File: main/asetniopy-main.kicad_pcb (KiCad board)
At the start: 2 copper layers, 32 x 33 mm, 19 parts, among them J1 Conn_01x02, J2 Conn_01x02, J3 Conn_01x02, J4 Conn_01x02, J5 Conn_01x02, J6 Power/Reset, J7 BAT+, J8 BAT-, U1 ProMicro, U2 LIS2DW12

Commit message: More parts, rotation/placement fixes.
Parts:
- turned C2 to -90 degrees
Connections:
- C2 pad 1: VCC -> GND
- C2 pad 2: GND -> VCC
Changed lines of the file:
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@@
   (net 12 "unconnected-(U1-Pad10)")
   (net 13 "unconnected-(U2-Pad5)")
-  (net 14 "Net-(U1-Pad24)")
+  (net 14 "Net-(J7-Pad1)")
   (net 15 "BAT-")
   (net 16 "RESET")
@@
       (net 1 "GND") (pinfunction "GND") (pintype "input"))
     (pad "24" thru_hole circle (at -13.97 -7.62 270) (size 1.7526 1.7526) (drill 1.0922) (layers *.Cu *.SilkS *.Mask)
-      (net 14 "Net-(U1-Pad24)") (pinfunction "RAW") (pintype "input"))
+      (net 14 "Net-(J7-Pad1)") (pinfunction "RAW") (pintype "input"))
     (model "/Users/danny/Documents/proj/custom-keyboard/kicad-libs/3d_models/ArduinoProMicro.wrl"
       (offset (xyz -13.96999979 -7.619999886 -5.841999912))
@@
     (fp_line (start -1.27 1.27) (end -1.27 -1.27) (layer "F.Fab") (width 0.1))
     (pad "1" thru_hole circle (at 0.0345 0) (size 1.7 1.7) (drill 1) (layers *.Cu *.Mask)
-      (net 14 "Net-(U1-Pad24)") (pinfunction "Pin_1") (pintype "passive"))
+      (net 14 "Net-(J7-Pad1)") (pinfunction "Pin_1") (pintype "passive"))
   )
   (footprint "MountingHole:MountingHole_2.2mm_M2_Pad" (layer "F.Cu")
@@
   )
   (footprint "Capacitor_Tantalum_SMD:CP_EIA-3216-18_Kemet-A" (layer "B.Cu")
-    (at 99.625 113.15 90)
+    (at 99.625 113.15 -90)
     (descr "Tantalum Capacitor SMD Kemet-A (3216-18 Metric), IPC_7351 nominal, (Body size from: http://www.kemet.com/Lists/ProductCatalog/Attachments/253/KEM_TC101_STD.pdf), generated with kicad-footprint-generator")
     (tags "capacitor tantalum")
+    (property "LCSC Part Number" "C7171")
     (property "Sheetfile" "asetniopy-main.kicad_sch")
     (property "Sheetname" "")
     (attr smd)
-    (fp_text reference "C2" (at -2.15 -2.075 180) (layer "B.SilkS")
+    (fp_text reference "C2" (at -2.15 -2.075) (layer "B.SilkS")
       (effects (font (size 1 1) (thickness 0.15)) (justify mirror))
     )
@@
     (fp_line (start -1.6 -0.8) (end 1.6 -0.8) (layer "B.Fab") (width 0.1))
     (fp_line (start 1.6 0.8) (end -1.2 0.8) (layer "B.Fab") (width 0.1))
-    (pad "1" smd roundrect (at -1.35 0 90) (size 1.4 1.35) (layers "B.Cu" "B.Paste" "B.Mask") (roundrect_rratio 0.185185)
+    (pad "1" smd roundrect (at -1.35 0 270) (size 1.4 1.35) (layers "B.Cu" "B.Paste" "B.Mask") (roundrect_rratio 0.185185)
+      (net 1 "GND") (pintype "passive"))
+    (pad "2" smd roundrect (at 1.35 0 270) (size 1.4 1.35) (layers "B.Cu" "B.Paste" "B.Mask") (roundrect_rratio 0.185185)
       (net 2 "VCC") (pintype "passive"))
-    (pad "2" smd roundrect (at 1.35 0 90) (size 1.4 1.35) (layers "B.Cu" "B.Paste" "B.Mask") (roundrect_rratio 0.185185)
-      (net 1 "GND") (pintype "passive"))
     (model "${KICAD6_3DMODEL_DIR}/Capacitor_Tantalum_SMD.3dshapes/CP_EIA-3216-18_Kemet-A.wrl"
       (offset (xyz 0 0 0))
@@
     (descr "LGA12")
     (tags "lga land grid array")
+    (property "LCSC Part Number" "C189624")
     (property "Sheetfile" "asetniopy-main.kicad_sch")
     (property "Sheetname" "")
@@
     (descr "Capacitor SMD 0603 (1608 Metric), square (rectangular) end terminal, IPC_7351 nominal, (Body size source: IPC-SM-782 page 76, https://www.pcb-3d.com/wordpress/wp-content/uploads/ipc-sm-782a_amendment_1_and_2.pdf), generated with kicad-footprint-generator")
     (tags "capacitor")
+    (property "LCSC Part Number" "C14663")
     (property "Sheetfile" "asetniopy-main.kicad_sch")
     (property "Sheetname" "")
@@
     (descr "Capacitor SMD 0603 (1608 Metric), square (rectangular) end terminal, IPC_7351 nominal, (Body size source: IPC-SM-782 page 76, https://www.pcb-3d.com/wordpress/wp-content/uploads/ipc-sm-782a_amendment_1_and_2.pdf), generated with kicad-footprint-generator")
     (tags "capacitor")
-    (property "Sheetfile" "asetniopy-main.kicad_sch")
-    (property "Sheetname" "")
+    (property "LCSC Part Number" "C14663")
+    (property "Sheetfile" "asetniopy-main.kicad_sch")
+    (property "Sheetname" "")

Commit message: Timestamps
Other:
- board text added: "By: @petejohanson Commit: ${COMMIT}"
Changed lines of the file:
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@@
     )
   )
+  (property "COMMIT" "deadbeef")
   (net 0 "")
   (net 1 "GND")
@@
   (gr_line (start 89 89.5) (end 87 89.5) (layer "Edge.Cuts") (width 0.1))
   (gr_arc (start 113 83.5) (mid 116 86.5) (end 113 89.5) (layer "Edge.Cuts") (width 0.1))
+  (gr_text "By:\n@petejohanson\nCommit:\n${COMMIT}" (at 98.975 104.625 90) (layer "F.SilkS")
+    (effects (font (size 1 1) (thickness 0.15)) (justify left))
+  )
   (via (at 110.225 115.475) (size 0.8) (drill 0.4) (layers "F.Cu" "B.Cu") (free) (net 1))
   (via (at 96.125 114.95) (size 0.8) (drill 0.4) (layers "F.Cu" "B.Cu") (free) (net 1))

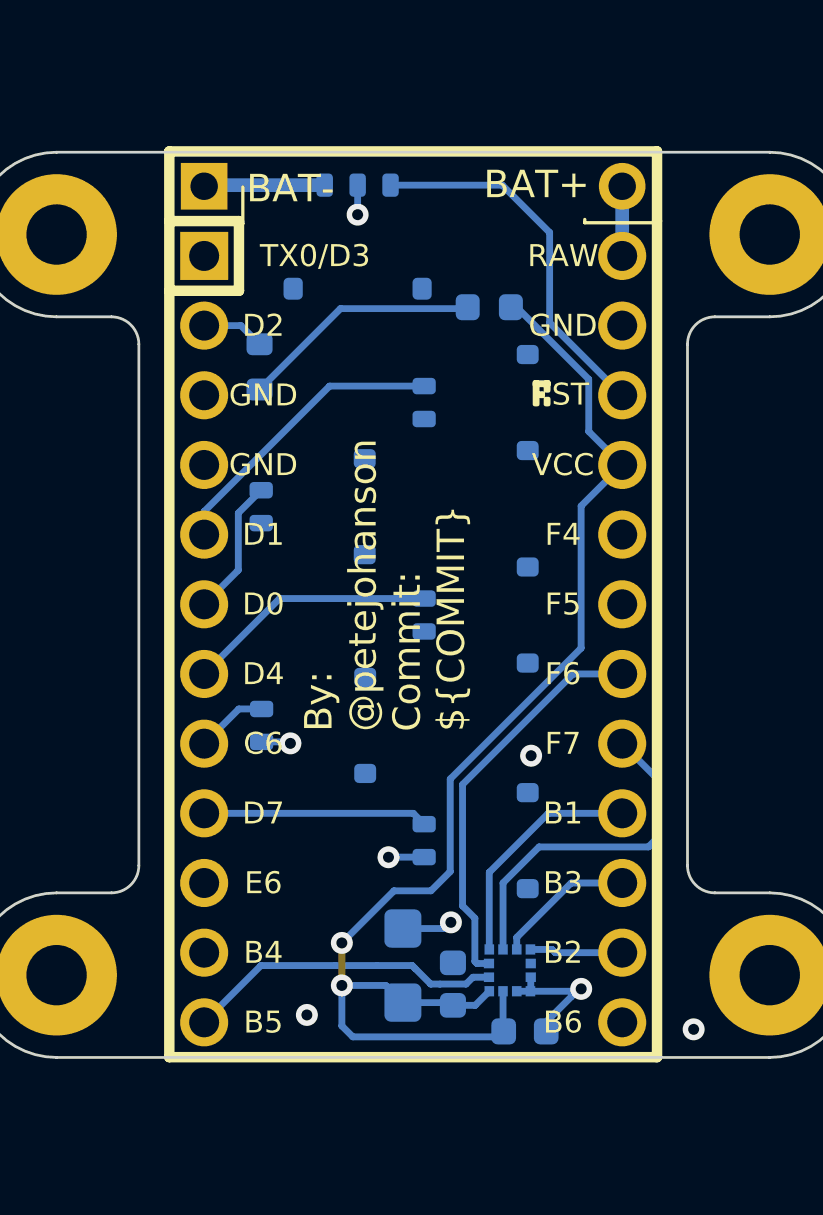
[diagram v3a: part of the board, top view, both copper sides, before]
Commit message: Minor placement/silk tweaks.
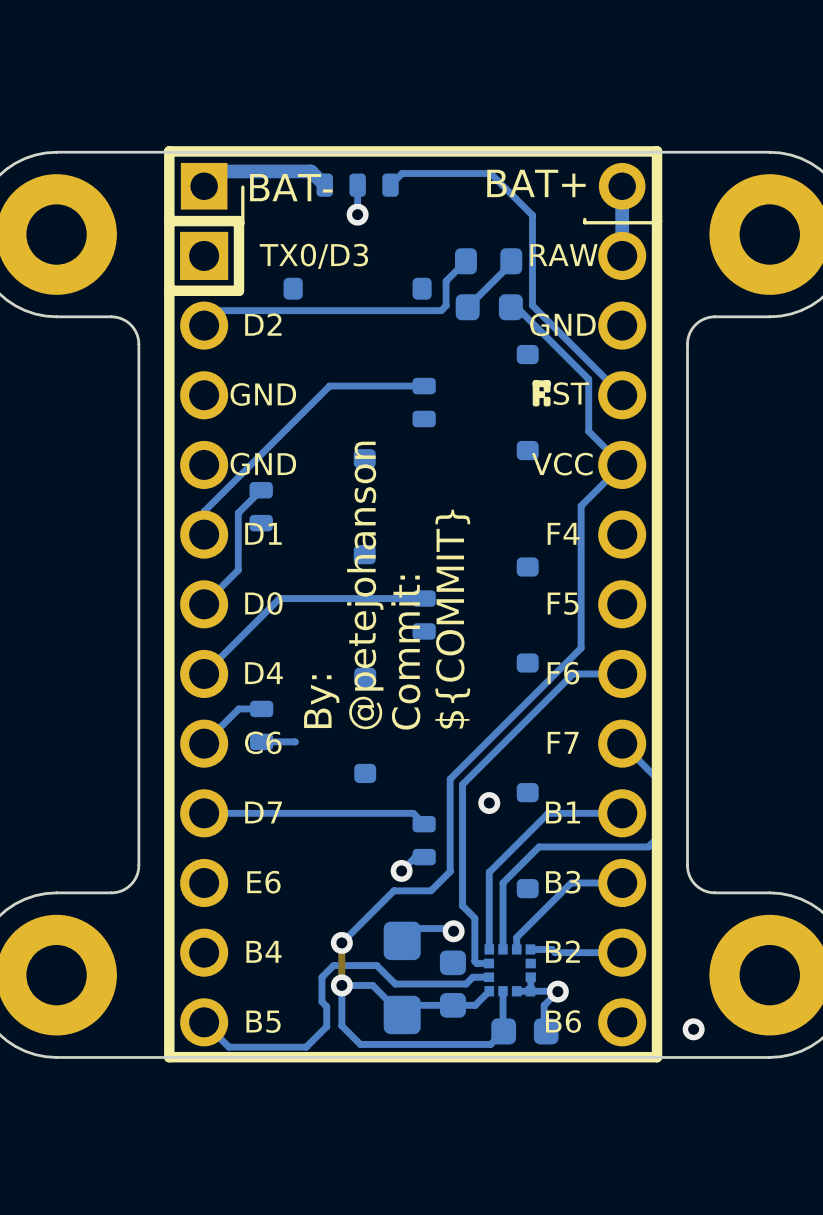
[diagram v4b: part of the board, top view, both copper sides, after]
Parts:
- D1: value User -> Blue
- R1: value 120 -> 68
- moved R1 9.19 mm to (102.8, 87.5), turned to 0 degrees
- moved C2 0.45 mm to (99.6, 113.6)
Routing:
- net LED: track 2.30 -> 11.0 mm
- net Net-(D1-Pad1): track 8.83 -> 2.33 mm
- net ACC_INT2: track 11.6 -> 13.7 mm
- net GND: track 10.6 -> 8.93 mm, vias 8 -> 6
- net VCC: track 46.3 -> 47.0 mm

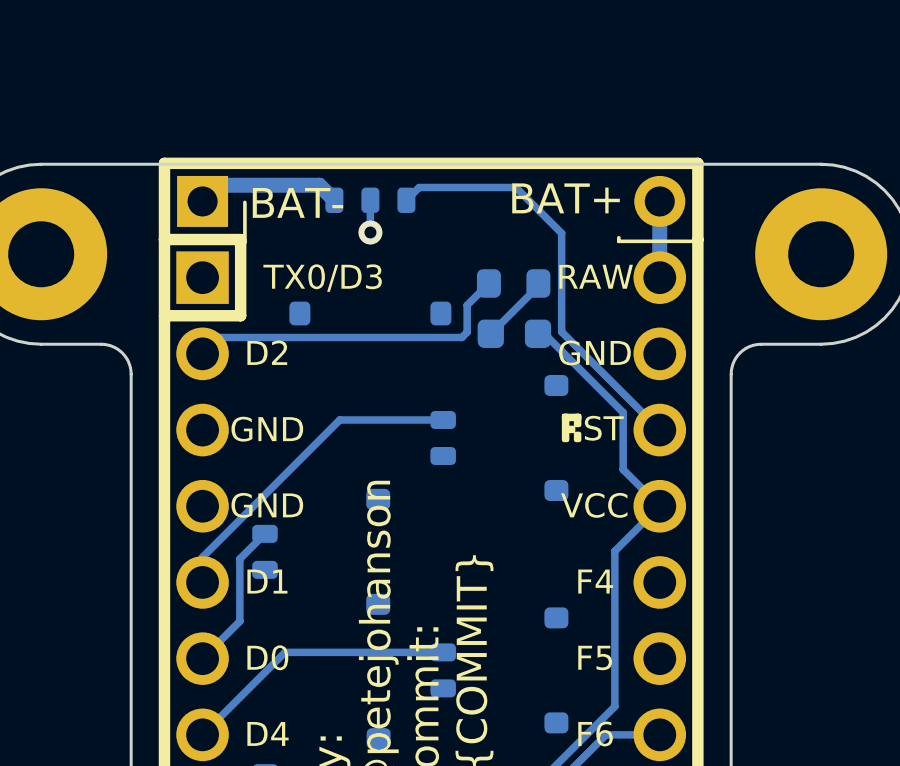
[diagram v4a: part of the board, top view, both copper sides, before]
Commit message: Switch to RGB LED.
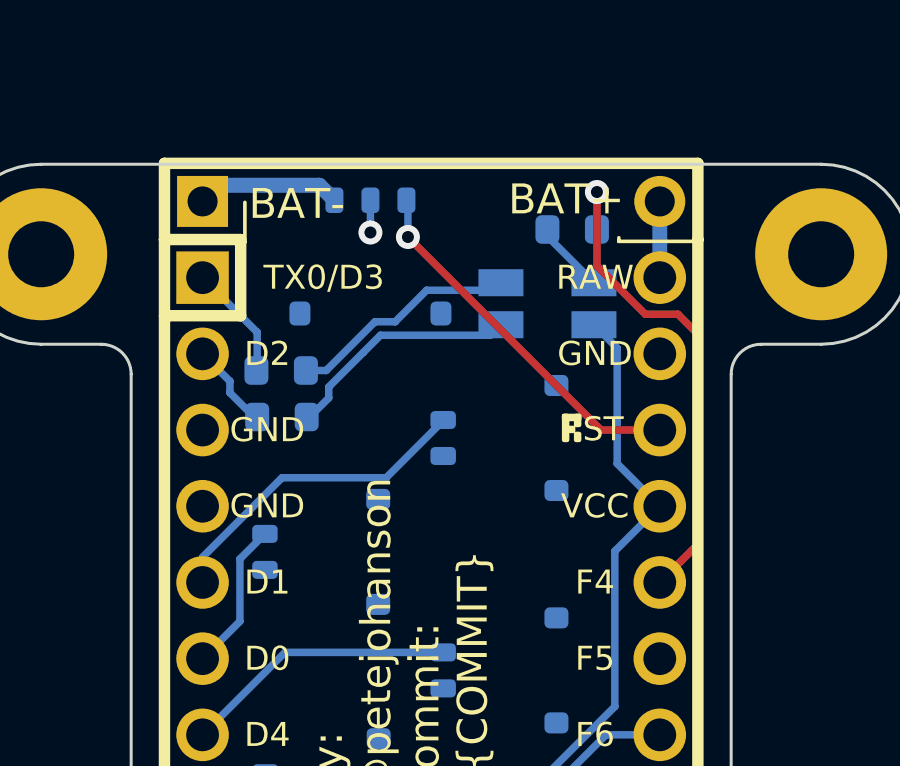
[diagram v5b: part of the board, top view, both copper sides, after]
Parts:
- added R2: 22, Resistor_SMD:R_0603_1608Metric, B.Cu at (95.0, 91.9)
- added R3: 22, Resistor_SMD:R_0603_1608Metric, B.Cu at (104.7, 85.7)
- D1: value Blue -> LED_ABGR; footprint LED_SMD:LED_0603_1608Metric -> LED_SMD:LED_RGB_Wuerth-PLCC4_3.2x2.8mm_150141M173100
- moved R1 8.27 mm to (95.0, 90.4)
- moved D1 1.49 mm to (103.9, 88.2)
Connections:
- D1 pad 1: Net-(D1-Pad1) -> VCC
- D1 pad 2: VCC -> Net-(D1-Pad2)
- R1 pad 1: LED -> LED_R
- R1 pad 2: Net-(D1-Pad1) -> Net-(R1-Pad2)
- U1 pad 1: unconnected-(U1-Pad1) -> LED_R
- U1 pad 2: LED -> LED_G
- U1 pad 20: unconnected-(U1-Pad20) -> LED_B
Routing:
- net LED_B: track 0.00 -> 16.8 mm, vias 0 -> 1
- net LED: track 11.0 -> 0.00 mm
- net Net-(D1-Pad3): track 0.00 -> 8.00 mm
- net Net-(R1-Pad2): track 0.00 -> 7.71 mm
- net LED_R: track 0.00 -> 3.95 mm
- net LED_G: track 0.00 -> 2.96 mm
- net Net-(D1-Pad2): track 0.00 -> 2.42 mm
- net Net-(D1-Pad1): track 2.33 -> 0.00 mm
- net RESET: track 13.9 -> 12.3 mm, vias 0 -> 1
- net VCC: track 47.0 -> 46.4 mm

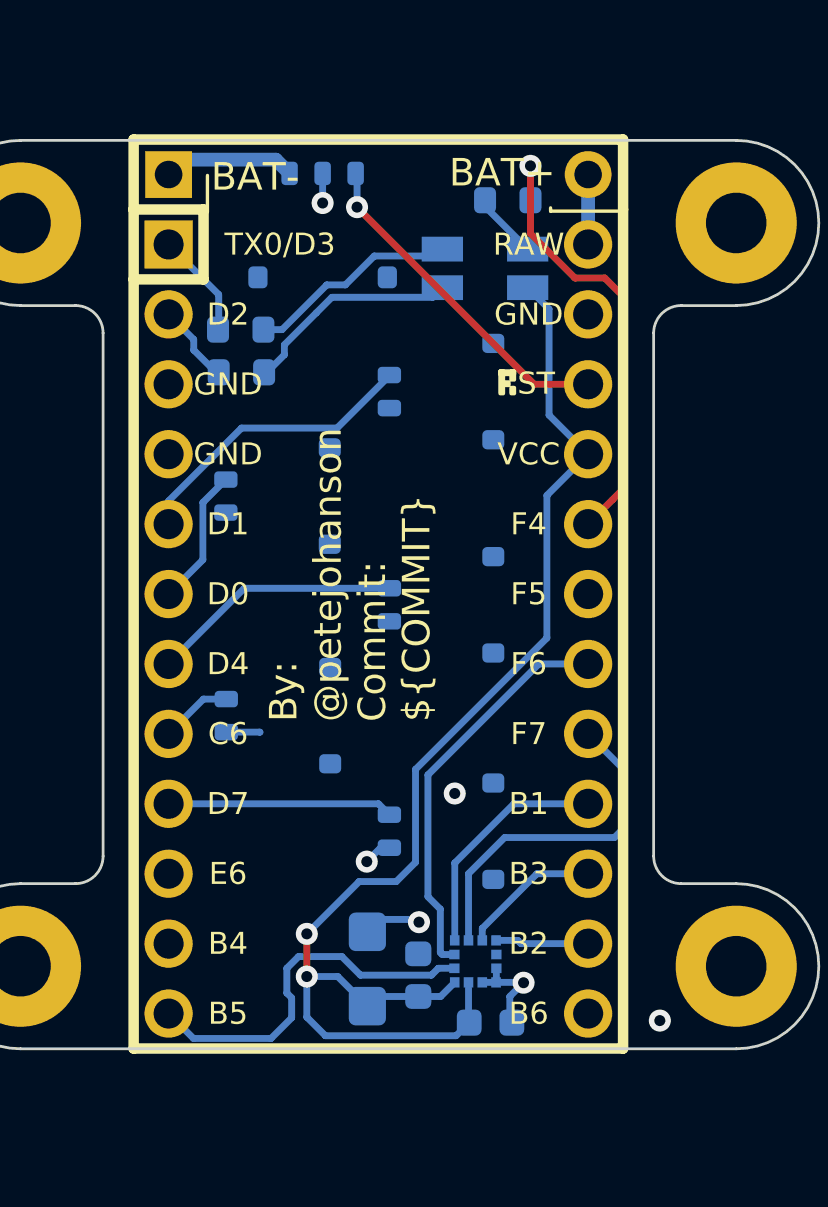
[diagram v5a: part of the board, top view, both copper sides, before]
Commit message: Move to LSM6DSO iNEMO IC.
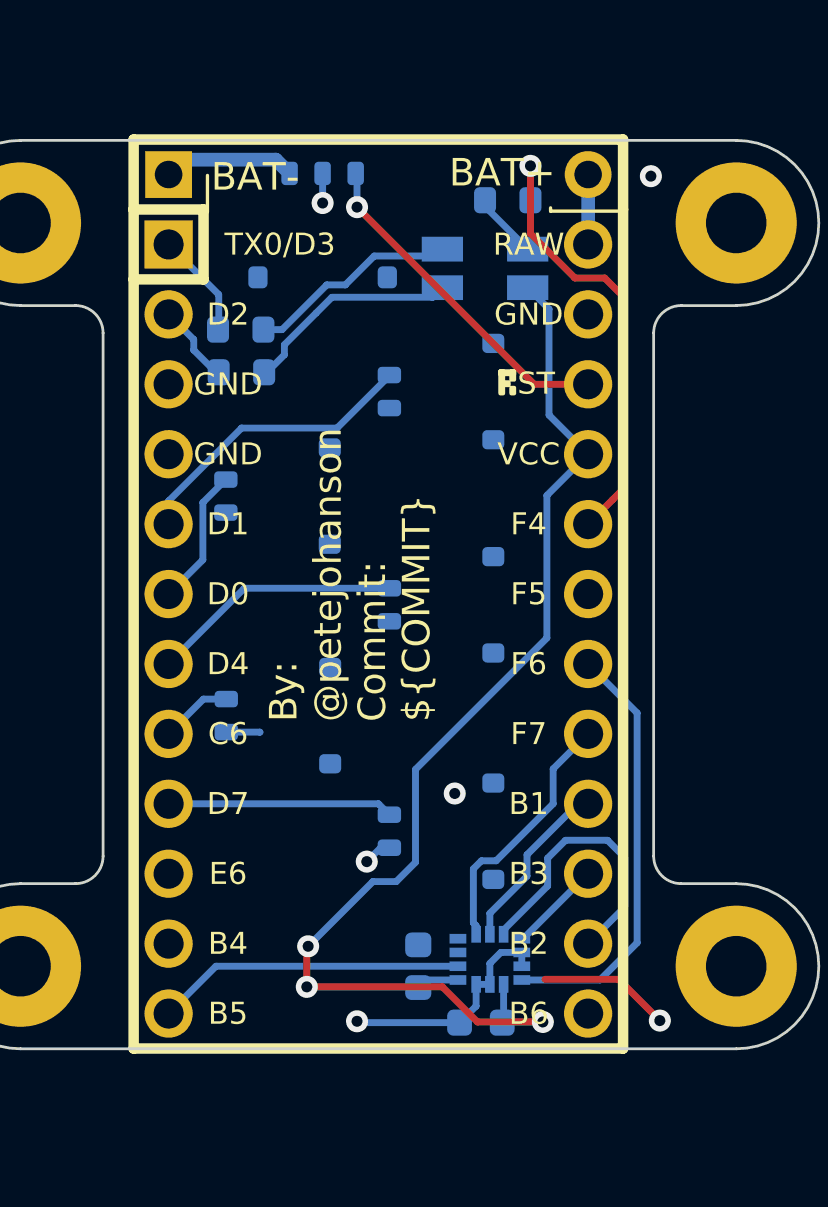
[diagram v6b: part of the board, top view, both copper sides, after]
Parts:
- removed C2: 10uF, Capacitor_Tantalum_SMD:CP_EIA-3216-18_Kemet-A
- U2: value LIS2DW12 -> LSM6DSO; footprint Package_LGA:LGA-12_2x2mm_P0.5mm -> main:PQFN50P250X300X86-14N
- moved U2 0.53 mm to (104.0, 113.2), turned to 180 degrees
- moved C1 0.35 mm to (103.7, 115.5), turned to 0 degrees
- moved C3 0.33 mm to (101.5, 113.5)
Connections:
- U2 pad 1: SCL -> CIPO
- U2 pad 10: VCC -> unconnected-(U2-Pad10)
- U2 pad 11: ACC_INT2 -> unconnected-(U2-Pad11)
- U2 pad 12: ACC_INT1 -> ACC_CS
- U2 pad 2: ACC_CS -> GND
- U2 pad 3: CIPO -> GND
- U2 pad 4: COPI -> ACC_INT1
- U2 pad 5: unconnected-(U2-Pad5) -> VCC
- U2 pad 8: GND -> VCC
- U2 pad 9: VCC -> ACC_INT2
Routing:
- net GND: track 8.93 -> 16.6 mm
- net COPI: track 3.39 -> 10.4 mm
- net ACC_CS: track 12.7 -> 9.36 mm
- net ACC_INT2: track 13.7 -> 11.2 mm
- net VCC: track 46.4 -> 48.7 mm, vias 2 -> 3
- net SCL: track 8.55 -> 6.44 mm
- net CIPO: track 5.10 -> 3.39 mm
- net ACC_INT1: track 14.7 -> 15.6 mm
